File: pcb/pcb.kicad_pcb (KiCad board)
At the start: 4 copper layers, 170.2 x 137.2 mm, 171 parts, among them J1 Barrel_Jack, J10 Screw_Terminal_01x08, J11 Conn_01x08_Male, J12 Conn_01x08_Male, J13 Conn_01x08_Male, J14 Conn_01x08_Male, J2 Barrel_Jack, J3 Screw_Terminal_01x02, J4 Screw_Terminal_01x02, J5 Conn_02x05_Odd_Even, J6 Conn_01x06_Male, J7 Screw_Terminal_01x08, J8 Screw_Terminal_01x08, J9 Screw_Terminal_01x08, SW1 SW_SPDT, U1 CPC5001G, U10 LTV-847, U11 LTV-847, U12 MCP23017-E_SP, U13 MCP23017-E_SP, U2 MCP23017-E_SP, U3 LTV-847, U4 LTV-847, U5 LTV-847, U6 LTV-847, U7 MCP23017-E_SP, U8 LTV-847, U9 LTV-847

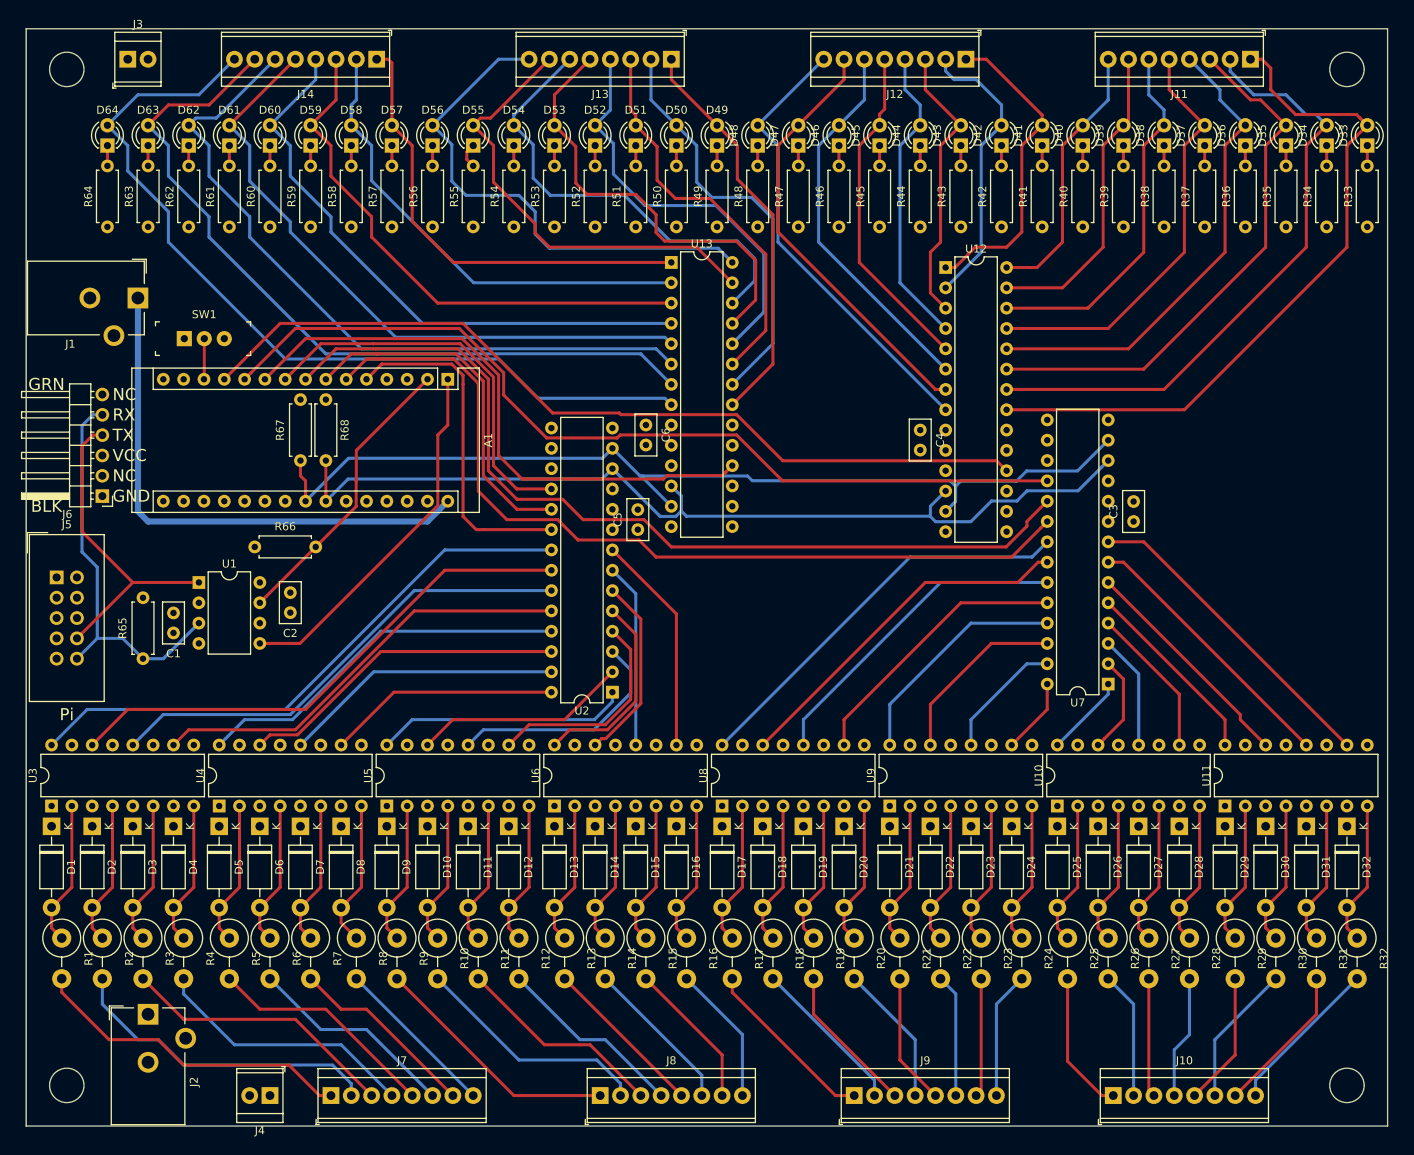
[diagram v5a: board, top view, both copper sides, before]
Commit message: Cleaning up some traces
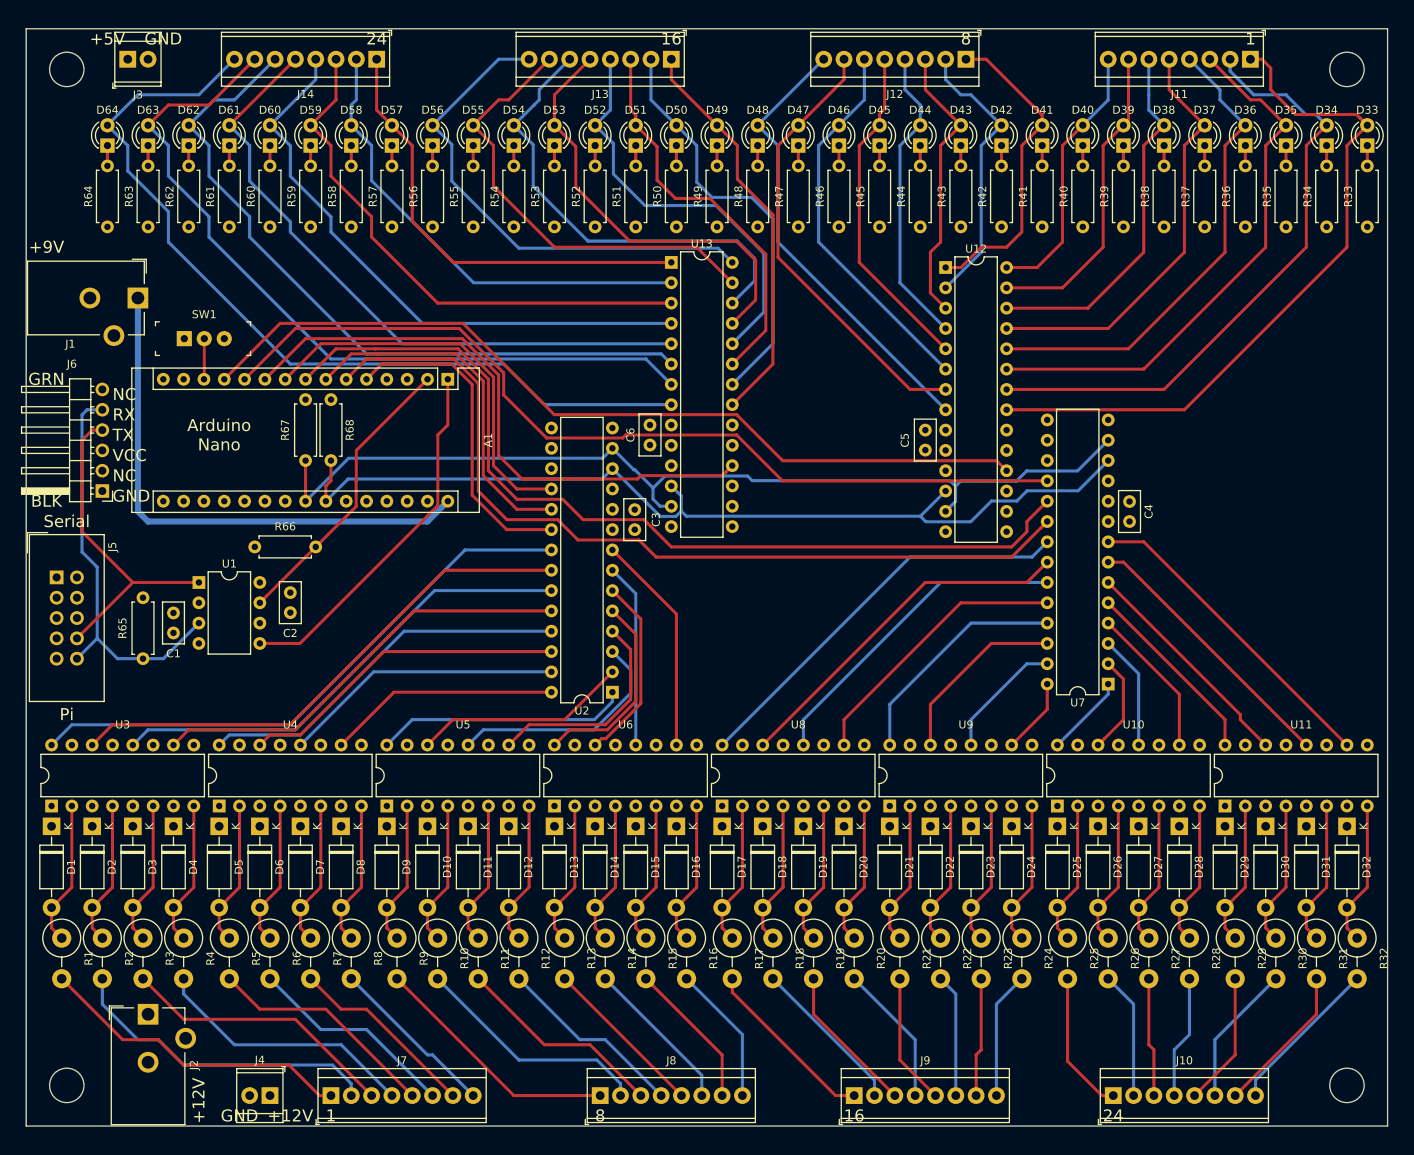
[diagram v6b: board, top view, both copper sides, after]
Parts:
- moved C3 62.4 mm to (159.9, 82.9)
- moved C5 38.0 mm to (196.2, 70.5), turned to 270 degrees
- moved C4 28.5 mm to (221.7, 81.9), turned to 90 degrees
- moved R67 0.64 mm to (118.7, 66.7)
- moved R68 0.64 mm to (121.9, 66.7)
- moved R8 0.64 mm to (124.5, 134.0)
- moved J6 0.63 mm to (93.3, 78.1)
- moved C6 0.51 mm to (161.8, 69.8)
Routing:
- net /INTA1: track 42.8 -> 40.6 mm
- net /Output 1/Out14: track 54.1 -> 56.0 mm
- net /Output 2/Out7: track 64.4 -> 62.7 mm
- net /TXout: track 49.7 -> 50.7 mm
- net /Output 2/Out4: track 55.3 -> 54.3 mm
- net /Input 1/Pin0: track 40.7 -> 39.7 mm
- net /Output 1/Out9: track 36.0 -> 35.1 mm
- net /Output 2/Out8: track 57.5 -> 56.6 mm
- net SCL: track 118.6 -> 119.4 mm
- net /RXout: track 40.9 -> 41.6 mm
- net Net-(D55-Pad1): track 3.20 -> 2.54 mm
- net /Input 1/Pin7: track 20.7 -> 21.3 mm
- net /Output 2/Out12: track 81.6 -> 82.2 mm
- net /Output 2/Out5: track 57.3 -> 57.9 mm
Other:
- board text added: "+12V"
- board text added: "+5V"
- board text added: "+9V"
- board text added: "1"
- board text added: "16"
- board text added: "24"
- board text added: "8"
- board text added: "Arduino Nano"
- board text added: "Serial"

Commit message: Silkscreen/tweaks/MSB switch/I2C header
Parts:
- added J15: Conn_01x02_Male, Connector_PinHeader_2.54mm:PinHeader_1x02_P2.54mm_Vertical, F.Cu at (249.6, 71.8)
- added SW2: SW_SPDT, digikey-footprints:Switch_Slide_11.6x4mm_EG1218, F.Cu at (249.6, 80.6)
- moved SW1 20.2 mm to (120.7, 48.3)
- moved R66 14.5 mm to (125.1, 92.1), turned to 90 degrees
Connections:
- A1 pad 14: Net-(A1-Pad14) -> /MSB
- SW1 pad 1: +5V -> Net-(SW1-Pad1)
- SW1 pad 3: GND -> Net-(SW1-Pad3)
- U12 pad 17: GND -> /MSB
- U13 pad 17: GND -> /MSB
- U2 pad 17: GND -> /MSB
- U7 pad 17: GND -> /MSB
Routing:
- net /MSB: track 0.00 -> 166.1 mm, vias 0 -> 1
- net SDA: track 121.4 -> 151.9 mm
- net SCL: track 119.4 -> 149.9 mm
- net /PRG_MODE: track 5.10 -> 26.0 mm
- net /RX: track 36.6 -> 39.2 mm
- net /Output 2/Out11: track 74.4 -> 77.0 mm
- net /Output 2/Out12: track 82.2 -> 83.7 mm
- net /Output 2/Out15: track 108.3 -> 107.6 mm
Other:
- board text added: "+12VDC"
- board text added: "+9VDC"
- board text added: "0"
- board text added: "0x20/0x24"
- board text added: "0x21/0x25"
- board text added: "0x22/0x26"
- board text added: "0x23/0x27"
- board text added: "Button pressed: connect to GND"
- board text added: "INTA1"
- board text added: "INTA2"
- board text added: "INTB1"
- board text added: "INTB2"
- board text added: "MODE"
- board text added: "MSB"
- board text added: "RST_IN1"
- board text added: "RST_IN2"
- board text added: "RST_OUT1"
- board text added: "RST_OUT2"
- board text added: "Rx"
- board text added: "SCL"
- board text added: "SDA"
- board text added: "Standaert Home Automation v1 2019"
- board text added: "Tx"
- board text added: "Vin"
- board text removed: "+9V"
